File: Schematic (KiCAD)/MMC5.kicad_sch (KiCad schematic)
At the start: 2 parts, among them K115 NAND_2, K116 INVERT

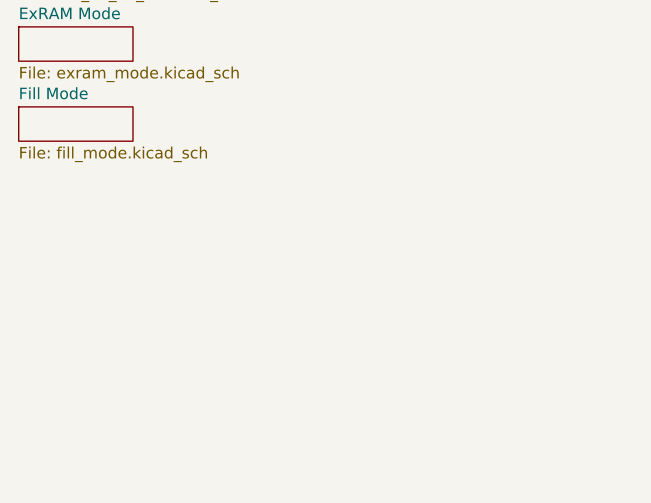
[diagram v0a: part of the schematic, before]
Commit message: - Started work on the pulse channels.  - Solved at least 2 of the red traces in the SVG.  - Finally realized that "Unknown 4to1" cells are actually just ordinary And-Or-Invert "AOI22" cells.
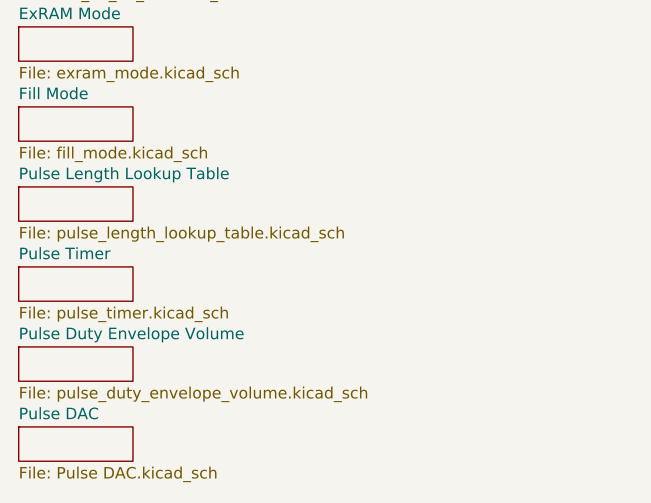
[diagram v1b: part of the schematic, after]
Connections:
- new net: K115. (X), K116. (X)
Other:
- added sheet Pulse DAC (Pulse DAC.kicad_sch)
- added sheet Pulse Duty Envelope Volume (pulse_duty_envelope_volume.kicad_sch)
- added sheet Pulse Length Lookup Table (pulse_length_lookup_table.kicad_sch)
- added sheet Pulse Timer (pulse_timer.kicad_sch)
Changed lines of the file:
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@@
+	)
+	(sheet
+		(at 17.78 161.29)
+		(size 12.7 3.81)
+		(exclude_from_sim no)
+		(in_bom yes)
+		(on_board yes)
+		(dnp no)
+		(fields_autoplaced yes)
+		(stroke
+			(width 0.1524)
+			(type solid)
+		)
+		(fill
+			(color 0 0 0 0.0000)
+		)
+		(property "Sheetname" "Pulse Duty Envelope Volume"
+			(at 17.78 160.5784 0)
+			(effects
+				(font
+					(size 1.27 1.27)
+				)
+				(justify left bottom)
+			)
+		)
+		(property "Sheetfile" "pulse_duty_envelope_volume.kicad_sch"
+			(at 17.78 165.6846 0)
+			(effects
+				(font
+					(size 1.27 1.27)
+				)
+				(justify left top)
+			)
+		)
+		(instances
+			(project "MMC5"
+				(path "/46093bf6-f83e-4237-9ece-7350a682aff0"
+					(page "18")
+				)
+			)
+		)
 	)
 	(sheet
@@
 	)
 	(sheet
+		(at 17.78 152.4)
+		(size 12.7 3.81)
+		(exclude_from_sim no)
+		(in_bom yes)
+		(on_board yes)
+		(dnp no)
+		(fields_autoplaced yes)
+		(stroke
+			(width 0.1524)
+			(type solid)
+		)
+		(fill
+			(color 0 0 0 0.0000)
+		)
+		(property "Sheetname" "Pulse Timer"
+			(at 17.78 151.6884 0)
+			(effects
+				(font
+					(size 1.27 1.27)
+				)
+				(justify left bottom)
+			)
+		)
+		(property "Sheetfile" "pulse_timer.kicad_sch"
+			(at 17.78 156.7946 0)
+			(effects
+				(font
+					(size 1.27 1.27)
+				)
+				(justify left top)
+			)
+		)
+		(instances
+			(project "MMC5"
+				(path "/46093bf6-f83e-4237-9ece-7350a682aff0"
+					(page "17")
+				)
+			)
+		)
+	)
+	(sheet
+		(at 17.78 170.18)
+		(size 12.7 3.81)
+		(exclude_from_sim no)
+		(in_bom yes)
+		(on_board yes)
+		(dnp no)
+		(fields_autoplaced yes)
+		(stroke
+			(width 0.1524)
+			(type solid)
+		)
+		(fill
+			(color 0 0 0 0.0000)
+		)
+		(property "Sheetname" "Pulse DAC"
+			(at 17.78 169.4684 0)
+			(effects
+				(font
+					(size 1.27 1.27)
+				)
+				(justify left bottom)
+			)
+		)
+		(property "Sheetfile" "Pulse DAC.kicad_sch"
+			(at 17.78 174.5746 0)
+			(effects
+				(font
+					(size 1.27 1.27)
+				)
+				(justify left top)
+			)
+		)
+		(instances
+			(project "MMC5"
+				(path "/46093bf6-f83e-4237-9ece-7350a682aff0"
+					(page "19")
+				)
+			)
+		)
+	)
+	(sheet
 		(at 17.78 134.62)
 		(size 12.7 3.81)
@@
 				)
 			)
+		)
+	)
+	(sheet
+		(at 17.78 143.51)
+		(size 12.7 3.81)
+		(exclude_from_sim no)
+		(in_bom yes)
+		(on_board yes)
+		(dnp no)
+		(fields_autoplaced yes)
+		(stroke
+			(width 0.1524)
+			(type solid)
+		)
+		(fill
+			(color 0 0 0 0.0000)
+		)
+		(property "Sheetname" "Pulse Length Lookup Table"
+			(at 17.78 142.7984 0)
+			(effects
+				(font
+					(size 1.27 1.27)
+				)
+				(justify left bottom)
+			)
+		)
+		(property "Sheetfile" "pulse_length_lookup_table.kicad_sch"
+			(at 17.78 147.9046 0)
+			(effects
+				(font
+					(size 1.27 1.27)
+				)
+				(justify left top)
+			)
+		)
+		(instances
+			(project "MMC5"
+				(path "/46093bf6-f83e-4237-9ece-7350a682aff0"
+					(page "16")
+				)
+			)

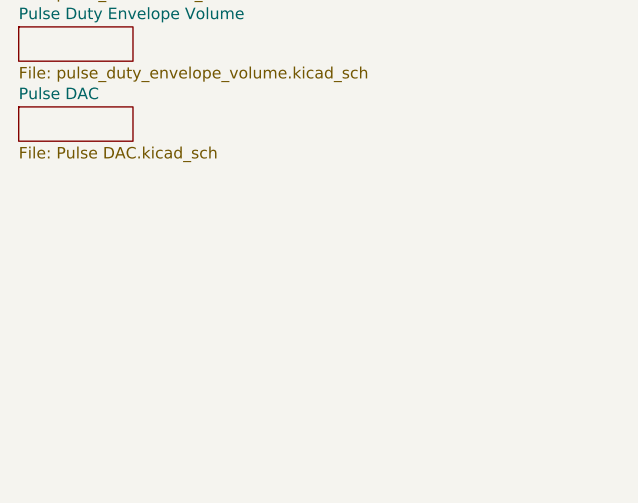
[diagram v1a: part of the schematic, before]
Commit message: Schematic Updates:  - Added all 10-bit CHR banking registers $5120 - $512B, including where all 10 bits come from when written.  - Added 8-bit CHR bank register $5202, which is the bank used when rendering the V-Split region.    + V-Split seems to always be 8-bit, 8kB bank regardless of CHR mode.  The wiki doesn't say that and I don't know for sure.  - Added decoding logic that activates the correct CHR bank for CHR A10, A11, A12 (corresponding to columns AV, AW, AX).  - Noted, AX15 activates $5202 CHR Bank for V-Split region.  AX16 activates CHR Bank from data stored in ExRAM for extended attributes.  Therefore, AX15 driven by AT1 High means we specifically are in v-split region, and not extended attribute mode.  With this knowledge, backtracking up the chain from AT1 to N14 sheds very useful insight what the 3-bit shift register at N11/N12/N13 is doing.  We now know that N14 goes low specifically for pattern table fetches when rendering the V-split region, and does not appear dual-purposed for extended attribute fetch sequencing.  This may seem rather subtle or unimportant, but it is a good advancement for higher level understanding what that mysterious shift register might be doing.
SVG Trace Updates:
 - Registers $5120, 5121, 5122, 5123 (first 4 CHR bank register), the outputs were labeled in reverse order.
 - Register $5130 (highest CHR bank bits), the outputs were labeled with backwards polarity.  The error was not having taken into account that the CPU data bus input to the latches came already inverted to begin with.
 - Still wrong: Cell AV7, 2-input NAND gate.  One of the inputs is missing and it logically should be driven by AS19 like the 4 cells to its direct right.  I can't quite make out how it makes that connection.
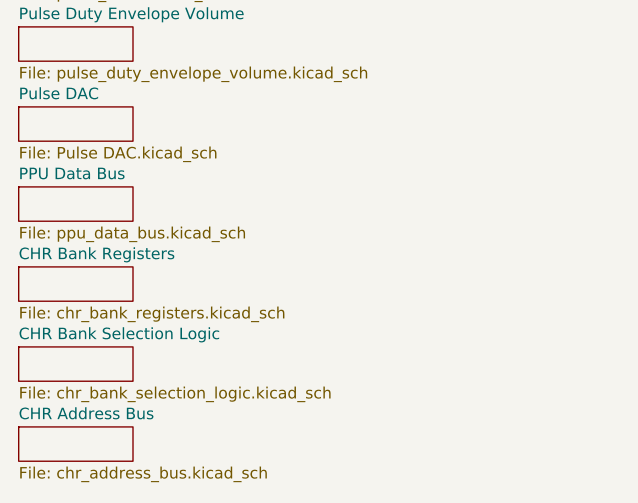
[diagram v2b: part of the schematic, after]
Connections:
- new net: K115. (X), K116. (X)
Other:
- added sheet CHR Address Bus (chr_address_bus.kicad_sch)
- added sheet CHR Bank Registers (chr_bank_registers.kicad_sch)
- added sheet CHR Bank Selection Logic (chr_bank_selection_logic.kicad_sch)
- added sheet PPU Data Bus (ppu_data_bus.kicad_sch)
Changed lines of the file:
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@@
+	)
+	(sheet
+		(at 17.78 196.85)
+		(size 12.7 3.81)
+		(exclude_from_sim no)
+		(in_bom yes)
+		(on_board yes)
+		(dnp no)
+		(fields_autoplaced yes)
+		(stroke
+			(width 0.1524)
+			(type solid)
+		)
+		(fill
+			(color 0 0 0 0.0000)
+		)
+		(property "Sheetname" "CHR Bank Selection Logic"
+			(at 17.78 196.1384 0)
+			(effects
+				(font
+					(size 1.27 1.27)
+				)
+				(justify left bottom)
+			)
+		)
+		(property "Sheetfile" "chr_bank_selection_logic.kicad_sch"
+			(at 17.78 201.2446 0)
+			(effects
+				(font
+					(size 1.27 1.27)
+				)
+				(justify left top)
+			)
+		)
+		(instances
+			(project "MMC5"
+				(path "/46093bf6-f83e-4237-9ece-7350a682aff0"
+					(page "22")
+				)
+			)
+		)
+	)
+	(sheet
+		(at 17.78 179.07)
+		(size 12.7 3.81)
+		(exclude_from_sim no)
+		(in_bom yes)
+		(on_board yes)
+		(dnp no)
+		(fields_autoplaced yes)
+		(stroke
+			(width 0.1524)
+			(type solid)
+		)
+		(fill
+			(color 0 0 0 0.0000)
+		)
+		(property "Sheetname" "PPU Data Bus"
+			(at 17.78 178.3584 0)
+			(effects
+				(font
+					(size 1.27 1.27)
+				)
+				(justify left bottom)
+			)
+		)
+		(property "Sheetfile" "ppu_data_bus.kicad_sch"
+			(at 17.78 183.4646 0)
+			(effects
+				(font
+					(size 1.27 1.27)
+				)
+				(justify left top)
+			)
+		)
+		(instances
+			(project "MMC5"
+				(path "/46093bf6-f83e-4237-9ece-7350a682aff0"
+					(page "20")
+				)
+			)
+		)
 	)
 	(sheet
@@
 	)
 	(sheet
+		(at 17.78 187.96)
+		(size 12.7 3.81)
+		(exclude_from_sim no)
+		(in_bom yes)
+		(on_board yes)
+		(dnp no)
+		(fields_autoplaced yes)
+		(stroke
+			(width 0.1524)
+			(type solid)
+		)
+		(fill
+			(color 0 0 0 0.0000)
+		)
+		(property "Sheetname" "CHR Bank Registers"
+			(at 17.78 187.2484 0)
+			(effects
+				(font
+					(size 1.27 1.27)
+				)
+				(justify left bottom)
+			)
+		)
+		(property "Sheetfile" "chr_bank_registers.kicad_sch"
+			(at 17.78 192.3546 0)
+			(effects
+				(font
+					(size 1.27 1.27)
+				)
+				(justify left top)
+			)
+		)
+		(instances
+			(project "MMC5"
+				(path "/46093bf6-f83e-4237-9ece-7350a682aff0"
+					(page "21")
+				)
+			)
+		)
+	)
+	(sheet
 		(at 17.78 152.4)
 		(size 12.7 3.81)
@@
 				)
 			)
+		)
+	)
+	(sheet
+		(at 17.78 205.74)
+		(size 12.7 3.81)
+		(exclude_from_sim no)
+		(in_bom yes)
+		(on_board yes)
+		(dnp no)
+		(fields_autoplaced yes)
+		(stroke
+			(width 0.1524)
+			(type solid)
+		)
+		(fill
+			(color 0 0 0 0.0000)
+		)
+		(property "Sheetname" "CHR Address Bus"
+			(at 17.78 205.0284 0)
+			(effects
+				(font
+					(size 1.27 1.27)
+				)
+				(justify left bottom)
+			)
+		)
+		(property "Sheetfile" "chr_address_bus.kicad_sch"
+			(at 17.78 210.1346 0)
+			(effects
+				(font
+					(size 1.27 1.27)
+				)
+				(justify left top)
+			)
+		)
+		(instances
+			(project "MMC5"
+				(path "/46093bf6-f83e-4237-9ece-7350a682aff0"
+					(page "23")
+				)
+			)

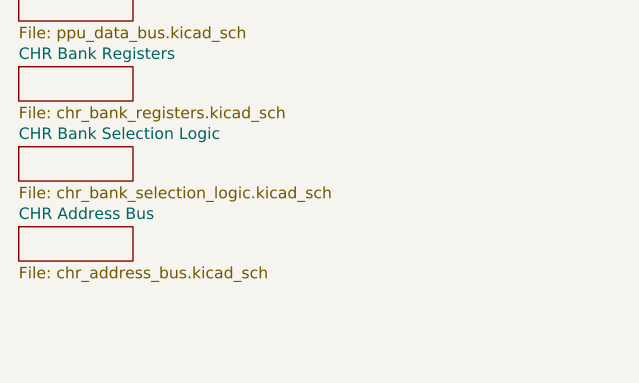
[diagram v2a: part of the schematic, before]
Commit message: - Finished up the CHR Ax bits.
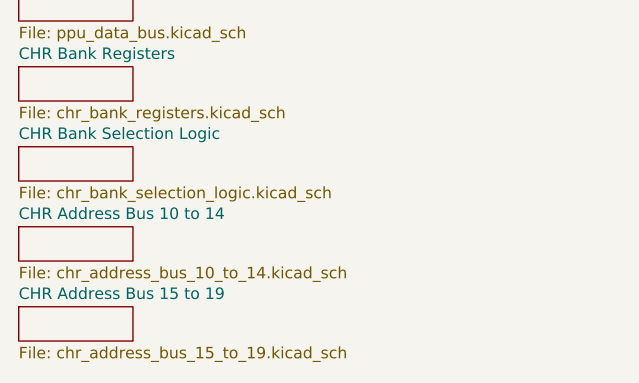
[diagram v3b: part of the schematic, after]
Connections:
- new net: K115. (X), K116. (X)
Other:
- sheet CHR Address Bus renamed CHR Address Bus 10 to 14
- added sheet CHR Address Bus 15 to 19 (chr_address_bus_15_to_19.kicad_sch)
- sheet CHR Address Bus 10 to 14: file chr_address_bus.kicad_sch -> chr_address_bus_10_to_14.kicad_sch
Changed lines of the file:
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@@
+	)
+	(sheet
+		(at 17.78 214.63)
+		(size 12.7 3.81)
+		(exclude_from_sim no)
+		(in_bom yes)
+		(on_board yes)
+		(dnp no)
+		(fields_autoplaced yes)
+		(stroke
+			(width 0.1524)
+			(type solid)
+		)
+		(fill
+			(color 0 0 0 0.0000)
+		)
+		(property "Sheetname" "CHR Address Bus 15 to 19"
+			(at 17.78 213.9184 0)
+			(effects
+				(font
+					(size 1.27 1.27)
+				)
+				(justify left bottom)
+			)
+		)
+		(property "Sheetfile" "chr_address_bus_15_to_19.kicad_sch"
+			(at 17.78 219.0246 0)
+			(effects
+				(font
+					(size 1.27 1.27)
+				)
+				(justify left top)
+			)
+		)
+		(instances
+			(project "MMC5"
+				(path "/46093bf6-f83e-4237-9ece-7350a682aff0"
+					(page "24")
+				)
+			)
+		)
 	)
 	(sheet
@@
 			(color 0 0 0 0.0000)
 		)
-		(property "Sheetname" "CHR Address Bus"
+		(property "Sheetname" "CHR Address Bus 10 to 14"
 			(at 17.78 205.0284 0)
 			(effects
@@
 			)
 		)
-		(property "Sheetfile" "chr_address_bus.kicad_sch"
+		(property "Sheetfile" "chr_address_bus_10_to_14.kicad_sch"
 			(at 17.78 210.1346 0)
 			(effects

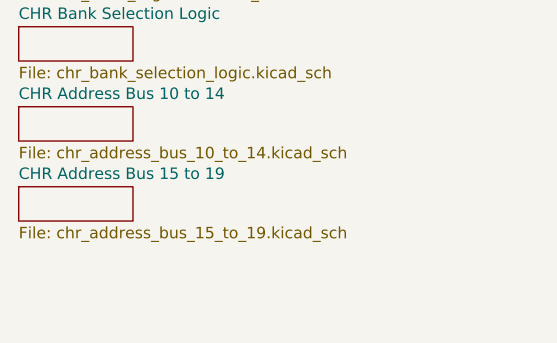
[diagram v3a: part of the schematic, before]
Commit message: - All cells in the left and center areas have now been added into the schematics.  - Changed naming of the PDF files; I was accidentally writing over furrtek's original with my new PDF.
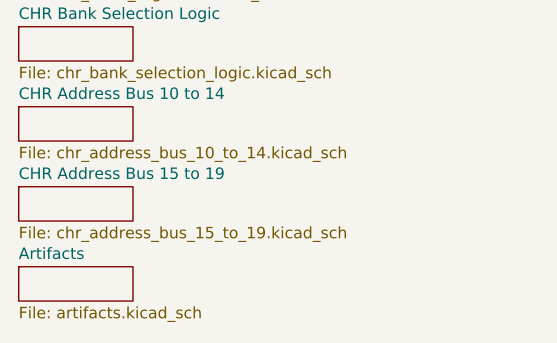
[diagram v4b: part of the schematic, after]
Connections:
- new net: K115. (X), K116. (X)
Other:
- added sheet Artifacts (artifacts.kicad_sch)
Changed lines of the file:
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@@
+	)
+	(sheet
+		(at 17.78 223.52)
+		(size 12.7 3.81)
+		(exclude_from_sim no)
+		(in_bom yes)
+		(on_board yes)
+		(dnp no)
+		(fields_autoplaced yes)
+		(stroke
+			(width 0.1524)
+			(type solid)
+		)
+		(fill
+			(color 0 0 0 0.0000)
+		)
+		(property "Sheetname" "Artifacts"
+			(at 17.78 222.8084 0)
+			(effects
+				(font
+					(size 1.27 1.27)
+				)
+				(justify left bottom)
+			)
+		)
+		(property "Sheetfile" "artifacts.kicad_sch"
+			(at 17.78 227.9146 0)
+			(effects
+				(font
+					(size 1.27 1.27)
+				)
+				(justify left top)
+			)
+		)
+		(instances
+			(project "MMC5"
+				(path "/46093bf6-f83e-4237-9ece-7350a682aff0"
+					(page "25")
+				)
+			)
+		)
 	)
 	(sheet

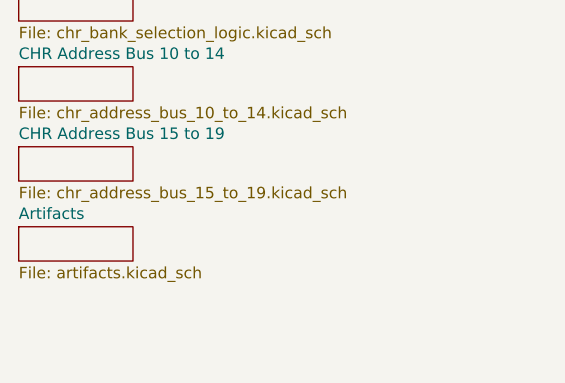
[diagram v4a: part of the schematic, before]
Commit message: - All known gates and traces are now accounted for in the schematics!  :)
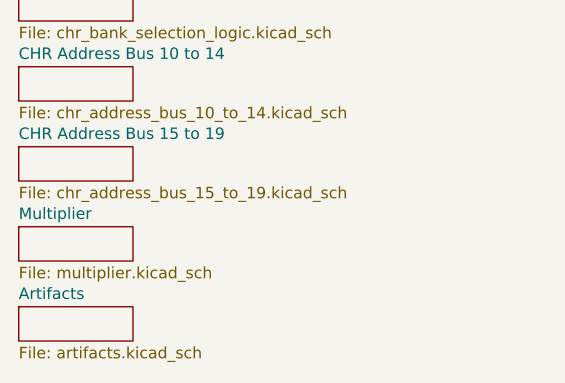
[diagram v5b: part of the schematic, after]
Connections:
- new net: K115. (X), K116. (X)
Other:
- added sheet Multiplier (multiplier.kicad_sch)
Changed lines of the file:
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@@
+	)
+	(sheet
+		(at 17.78 223.52)
+		(size 12.7 3.81)
+		(exclude_from_sim no)
+		(in_bom yes)
+		(on_board yes)
+		(dnp no)
+		(fields_autoplaced yes)
+		(stroke
+			(width 0.1524)
+			(type solid)
+		)
+		(fill
+			(color 0 0 0 0.0000)
+		)
+		(property "Sheetname" "Multiplier"
+			(at 17.78 222.8084 0)
+			(effects
+				(font
+					(size 1.27 1.27)
+				)
+				(justify left bottom)
+			)
+		)
+		(property "Sheetfile" "multiplier.kicad_sch"
+			(at 17.78 227.9146 0)
+			(effects
+				(font
+					(size 1.27 1.27)
+				)
+				(justify left top)
+			)
+		)
+		(instances
+			(project "MMC5"
+				(path "/46093bf6-f83e-4237-9ece-7350a682aff0"
+					(page "25")
+				)
+			)
+		)
 	)
 	(sheet
@@
 	)
 	(sheet
-		(at 17.78 223.52)
+		(at 17.78 232.41)
 		(size 12.7 3.81)
 		(exclude_from_sim no)
@@
 		)
 		(property "Sheetname" "Artifacts"
-			(at 17.78 222.8084 0)
+			(at 17.78 231.6984 0)
 			(effects
 				(font
@@
 		)
 		(property "Sheetfile" "artifacts.kicad_sch"
-			(at 17.78 227.9146 0)
-			(effects
-				(font
-					(size 1.27 1.27)
-				)
-				(justify left top)
-			)
-		)
-		(instances
-			(project "MMC5"
-				(path "/46093bf6-f83e-4237-9ece-7350a682aff0"
-					(page "25")
-				)
-			)
+			(at 17.78 236.8046 0)
+			(effects
+				(font
+					(size 1.27 1.27)
+				)
+				(justify left top)
+			)
+		)
+		(instances
+			(project "MMC5"
+				(path "/46093bf6-f83e-4237-9ece-7350a682aff0"
+					(page "26")
+				)
+			)
